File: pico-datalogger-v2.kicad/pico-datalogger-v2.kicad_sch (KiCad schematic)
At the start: 28 parts, among them J1 JST-PH2 Bat, J2 Conn_Pico_Left, J3 Conn_Pico_Right, J4 Alt-Bat, J6 Conn_Display_SPI, J8 Conn_ADC, J9 Conn_UART, Q1 AO3401A, SW1 SW_Push_SLIM, SW2 SW_Reset, U1 74LVC2G74, U2 PCF8523T, U3 Pico, U4 XTSD, Y1 Crystal

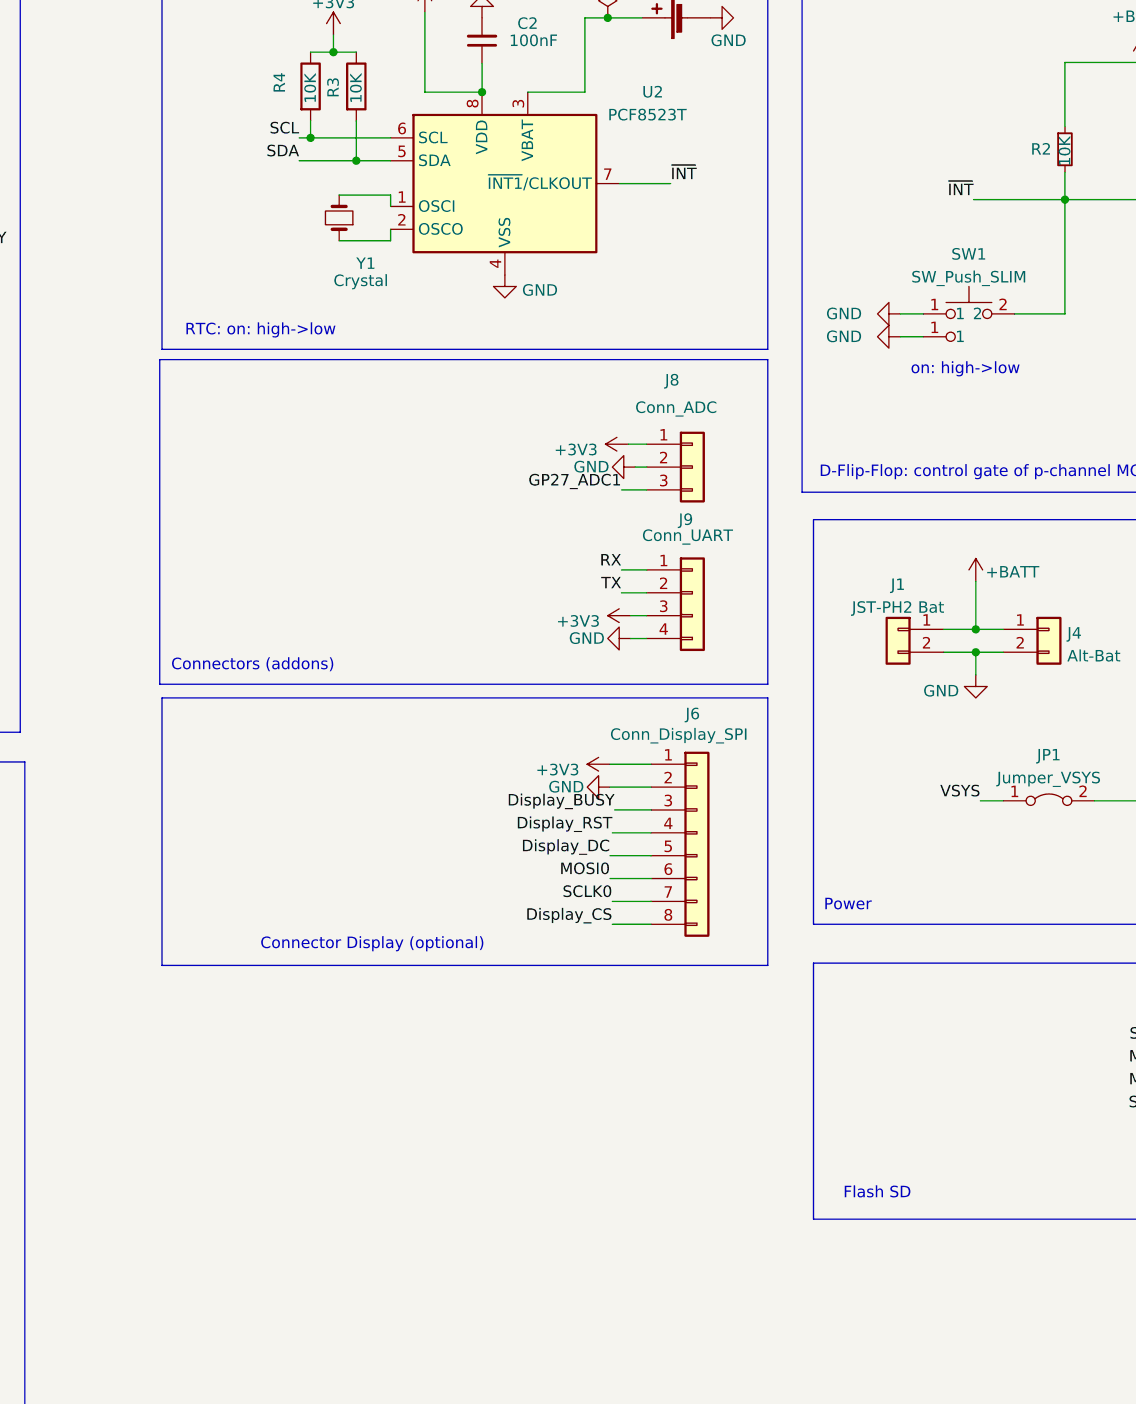
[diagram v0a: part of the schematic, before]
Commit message: added connectors
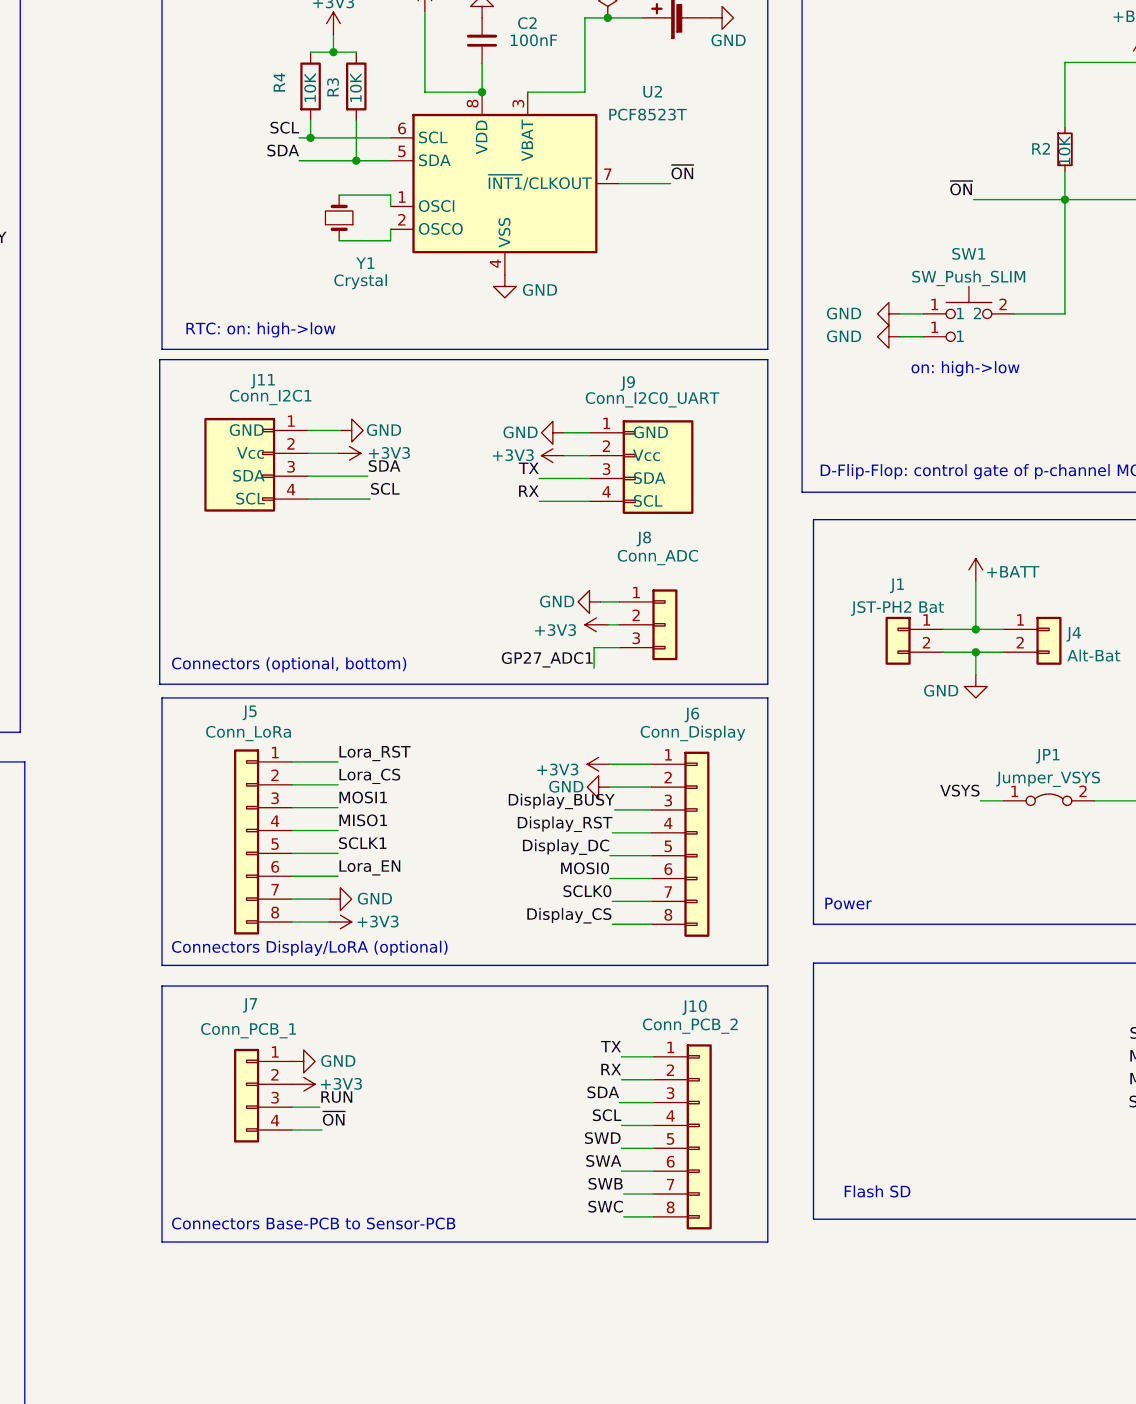
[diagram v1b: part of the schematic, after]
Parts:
- added J10: Conn_PCB_2, Connector_JST:JST_SUR_SM08B-SURS-TF_1x08-1MP_P0.80mm_Horizontal, symbol Connector_Generic:Conn_01x08
- added J11: Conn_I2C1, Connector_JST:JST_SH_SM04B-SRSS-TB_1x04-1MP_P1.00mm_Horizontal, symbol user:Stemma-QT_Qwicc
- added J5: Conn_LoRa, Connector_JST:JST_SUR_SM08B-SURS-TF_1x08-1MP_P0.80mm_Horizontal, symbol Connector_Generic:Conn_01x08
- added J7: Conn_PCB_1, Connector_JST:JST_SUR_SM04B-SURS-TF_1x04-1MP_P0.80mm_Horizontal, symbol Connector_Generic:Conn_01x04
- J6: value Conn_Display_SPI -> Conn_Display; footprint Connector_PinHeader_2.54mm:PinHeader_1x09_P2.54mm_Vertical -> Connector_JST:JST_SUR_SM08B-SURS-TF_1x08-1MP_P0.80mm_Horizontal
- J8: footprint Connector_PinHeader_2.54mm:PinHeader_1x03_P2.54mm_Horizontal -> Connector_JST:JST_PH_S3B-PH-SM4-TB_1x03-1MP_P2.00mm_Horizontal
- J9: value Conn_UART -> Conn_I2C0_UART; footprint Connector_PinHeader_2.54mm:PinHeader_1x04_P2.54mm_Horizontal -> Connector_JST:JST_SH_SM04B-SRSS-TB_1x04-1MP_P1.00mm_Horizontal; symbol Connector_Generic:Conn_01x04 -> user:Stemma-QT_Qwicc; now in the parts list
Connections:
- net +3V3: now also J8.2 (Pin_2), J9.2 (Vcc), J11.2 (Vcc), J5.8 (Pin_8), J7.2 (Pin_2); no longer J8.1 (Pin_1), J9.3 (Pin_3)
- net GND: now also J8.1 (Pin_1), J9.1 (GND), J11.1 (GND), J5.7 (Pin_7), J7.1 (Pin_1); no longer J8.2 (Pin_2), J9.4 (Pin_4)
- net Lora_CS: now also J5.2 (Pin_2)
- net Lora_EN: now also J5.6 (Pin_6)
- net Lora_RST: now also J5.1 (Pin_1)
- net MISO1: now also J5.4 (Pin_4)
- net MOSI1: now also J5.3 (Pin_3)
- net RUN: now also J7.3 (Pin_3)
- net RX: now also J9.4 (SCL), J10.2 (Pin_2); no longer J9.1 (Pin_1)
- net SCL: now also J10.4 (Pin_4), J11.4 (SCL)
- net SCLK1: now also J5.5 (Pin_5)
- net SDA: now also J10.3 (Pin_3), J11.3 (SDA)
- net SWA: now also J10.6 (Pin_6)
- net SWB: now also J10.7 (Pin_7)
- net SWC: now also J10.8 (Pin_8)
- net SWD: now also J10.5 (Pin_5)
- net TX: now also J9.3 (SDA), J10.1 (Pin_1); no longer J9.2 (Pin_2)
- net ~{INT} renamed ~{ON}
- net ~{ON}: now also J7.4 (Pin_4)
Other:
- note added: "Connectors (optional, bottom)"
- note added: "Connectors Base-PCB to Sensor-PCB"
- note added: "Connectors Display/LoRA (optional)"
- note removed: "Connector Display (optional)"
- note removed: "Connectors (addons)"
- moved on the sheet: J8

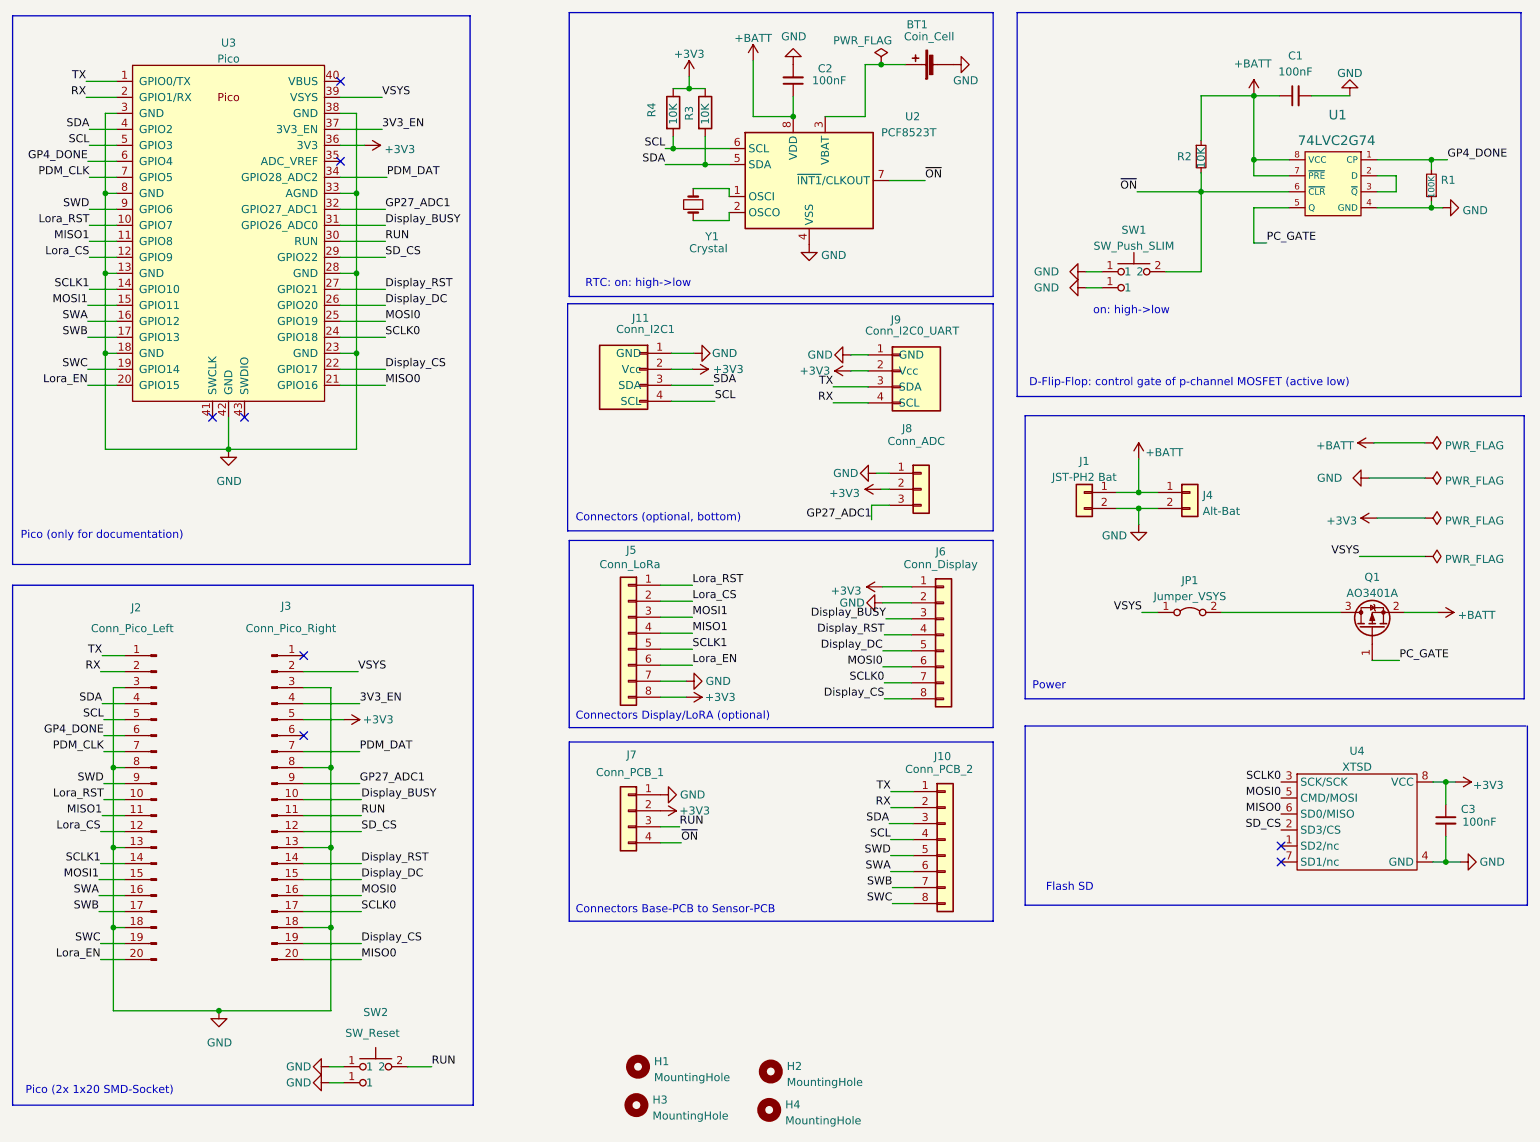
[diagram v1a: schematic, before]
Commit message: cleanup of connectors
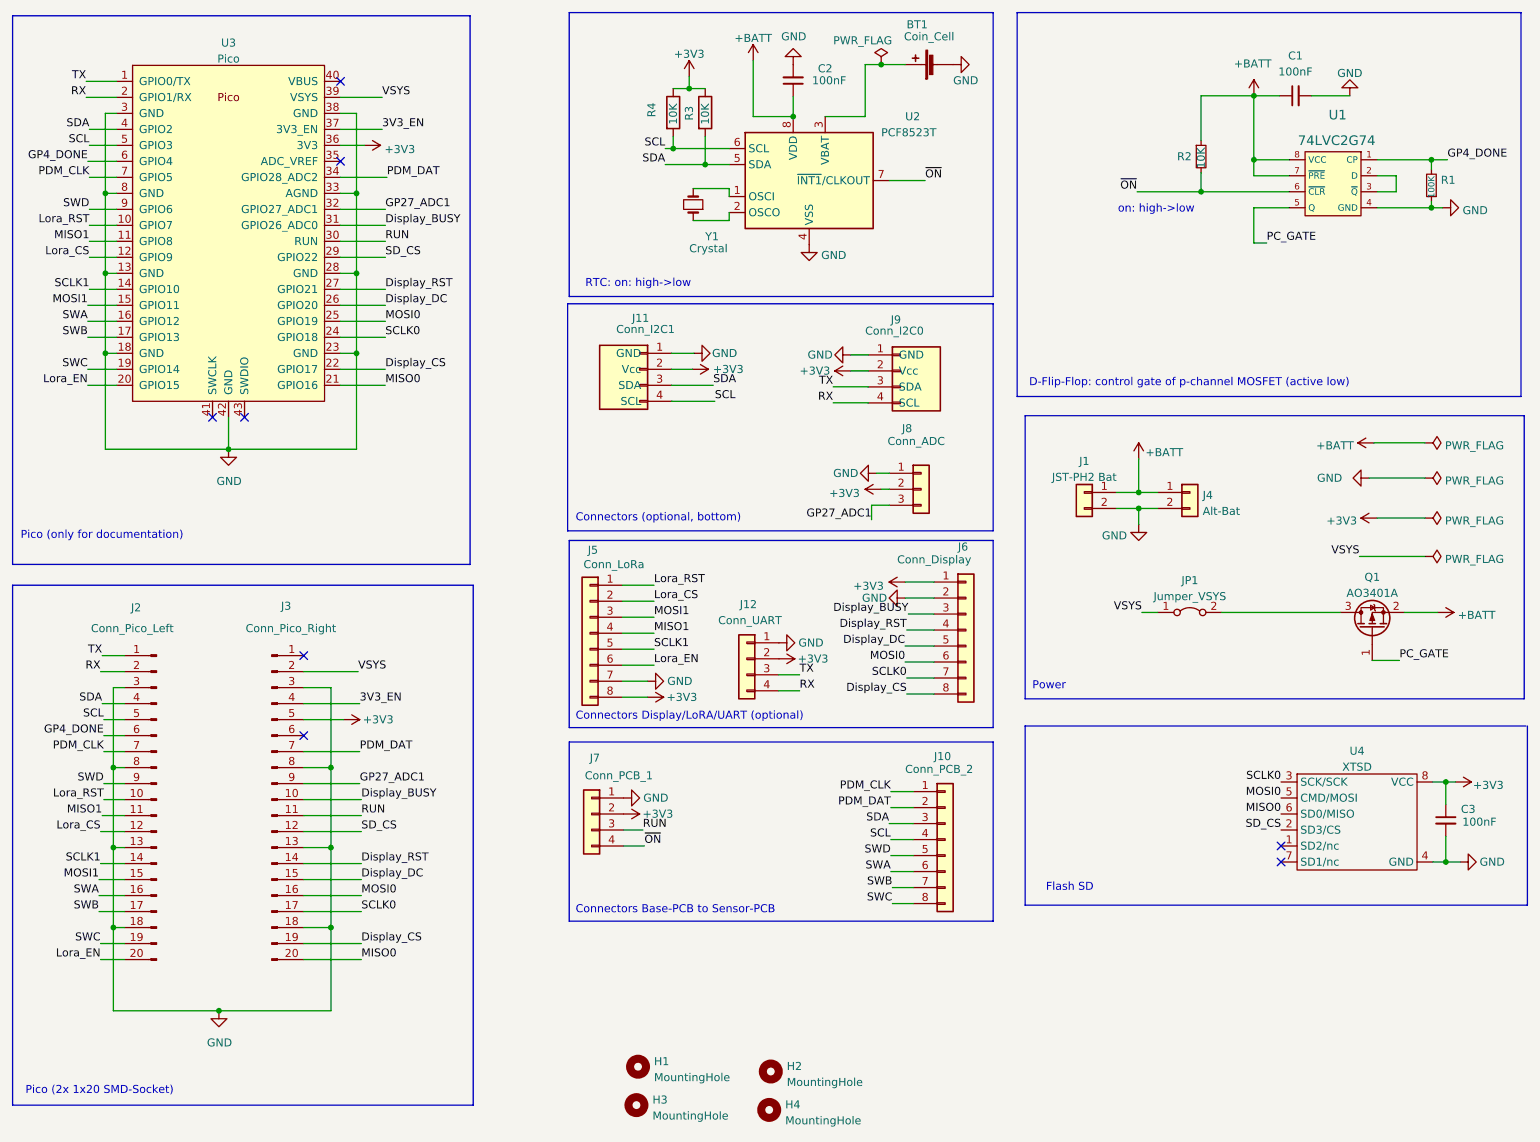
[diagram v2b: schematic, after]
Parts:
- removed SW1: SW_Push_SLIM, user:SW_PUSH_SLIM_1x4, symbol user:SW_Push_SLIM
- removed SW2: SW_Reset, user:SW_PUSH_SLIM_1x4, symbol user:SW_Push_SLIM
- added J12: Conn_UART, Connector_PinHeader_2.54mm:PinHeader_1x04_P2.54mm_Horizontal, symbol Connector_Generic:Conn_01x04
- J10, J5, J6: footprint Connector_JST:JST_SUR_SM08B-SURS-TF_1x08-1MP_P0.80mm_Horizontal -> Connector_JST:JST_SUR_BM08B-SURS-TF_1x08-1MP_P0.80mm_Vertical
- J7: footprint Connector_JST:JST_SUR_SM04B-SURS-TF_1x04-1MP_P0.80mm_Horizontal -> Connector_JST:JST_SUR_BM04B-SURS-TF_1x04-1MP_P0.80mm_Vertical
- J9: value Conn_I2C0_UART -> Conn_I2C0
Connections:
- net +3V3: now also J12.2 (Pin_2)
- net GND: now also J12.1 (Pin_1)
- net PDM_CLK: now also J10.1 (Pin_1)
- net PDM_DAT: now also J10.2 (Pin_2)
- net RX: now also J12.4 (Pin_4); no longer J10.2 (Pin_2)
- net TX: now also J12.3 (Pin_3); no longer J10.1 (Pin_1)
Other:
- note added: "Connectors Display/LoRA/UART (optional)"
- note removed: "Connectors Display/LoRA (optional)"
- moved on the sheet: J5, J6, J7
